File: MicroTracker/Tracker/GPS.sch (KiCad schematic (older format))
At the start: 27 parts, among them Q1 BC237, U2 GP.1575.15.4.B.02, U3 TPS22943, U8 BGA725L6, U9 TESEO-LIV3F

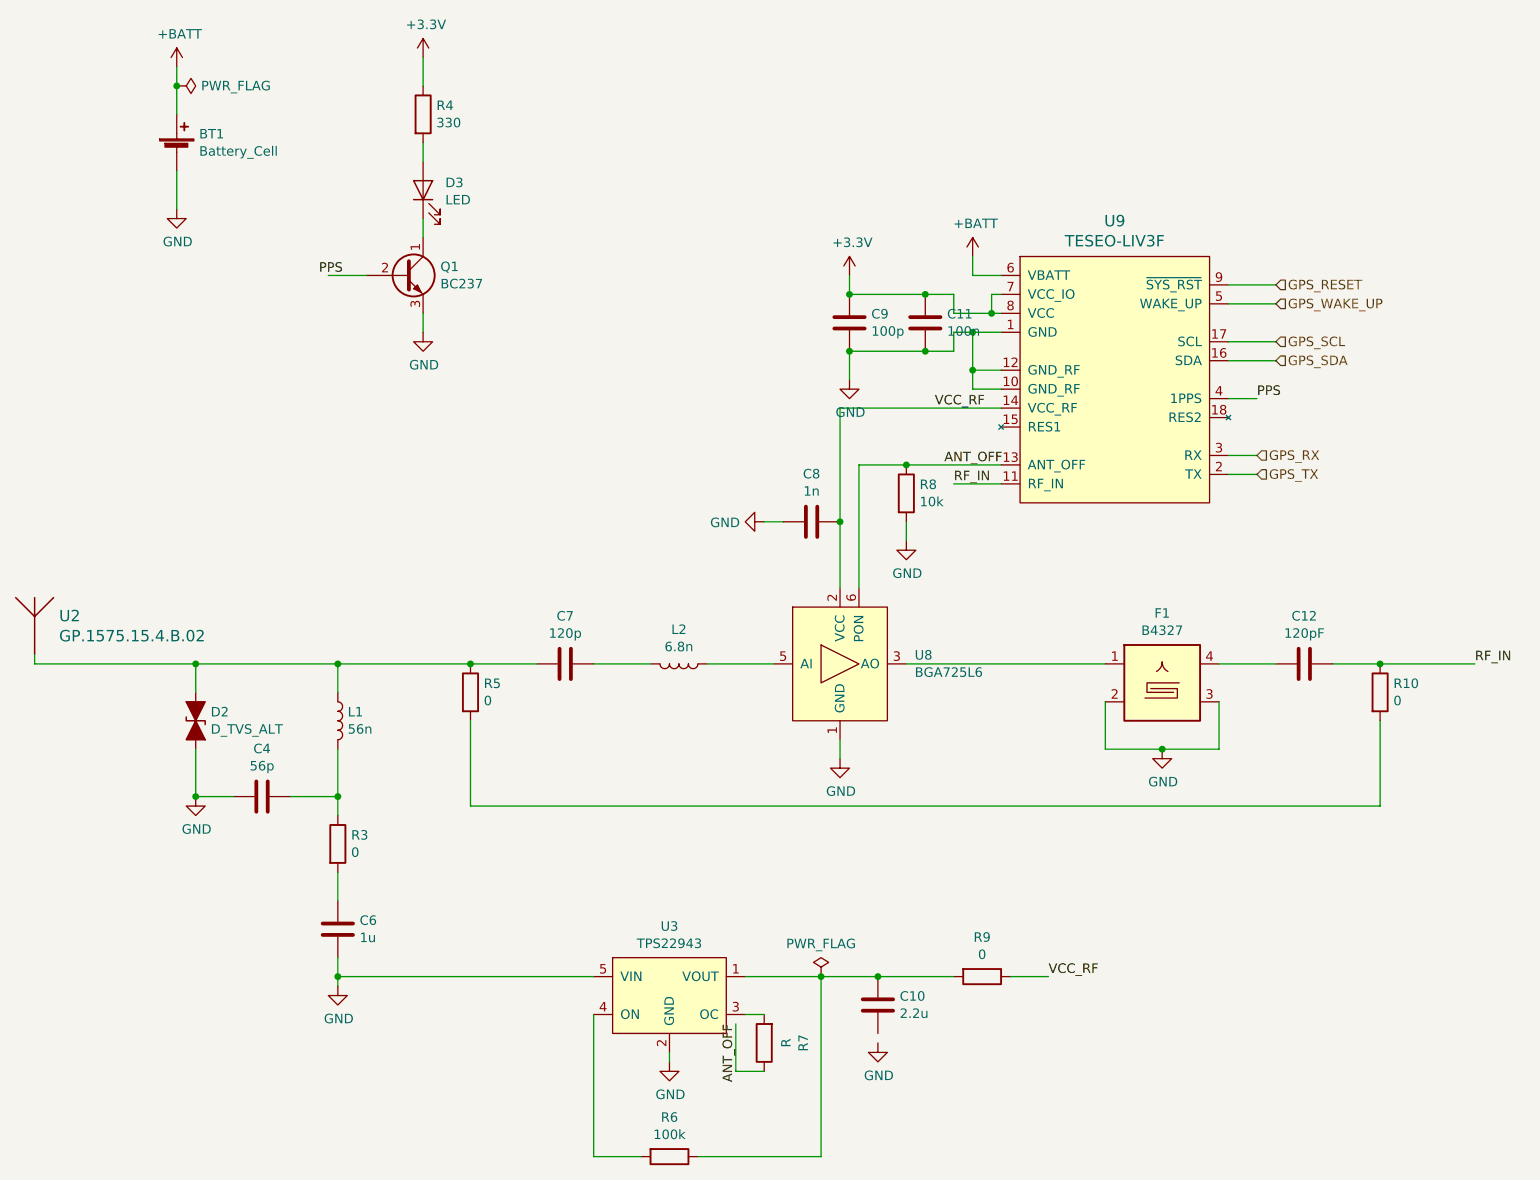
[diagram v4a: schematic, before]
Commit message: added more parts and lib
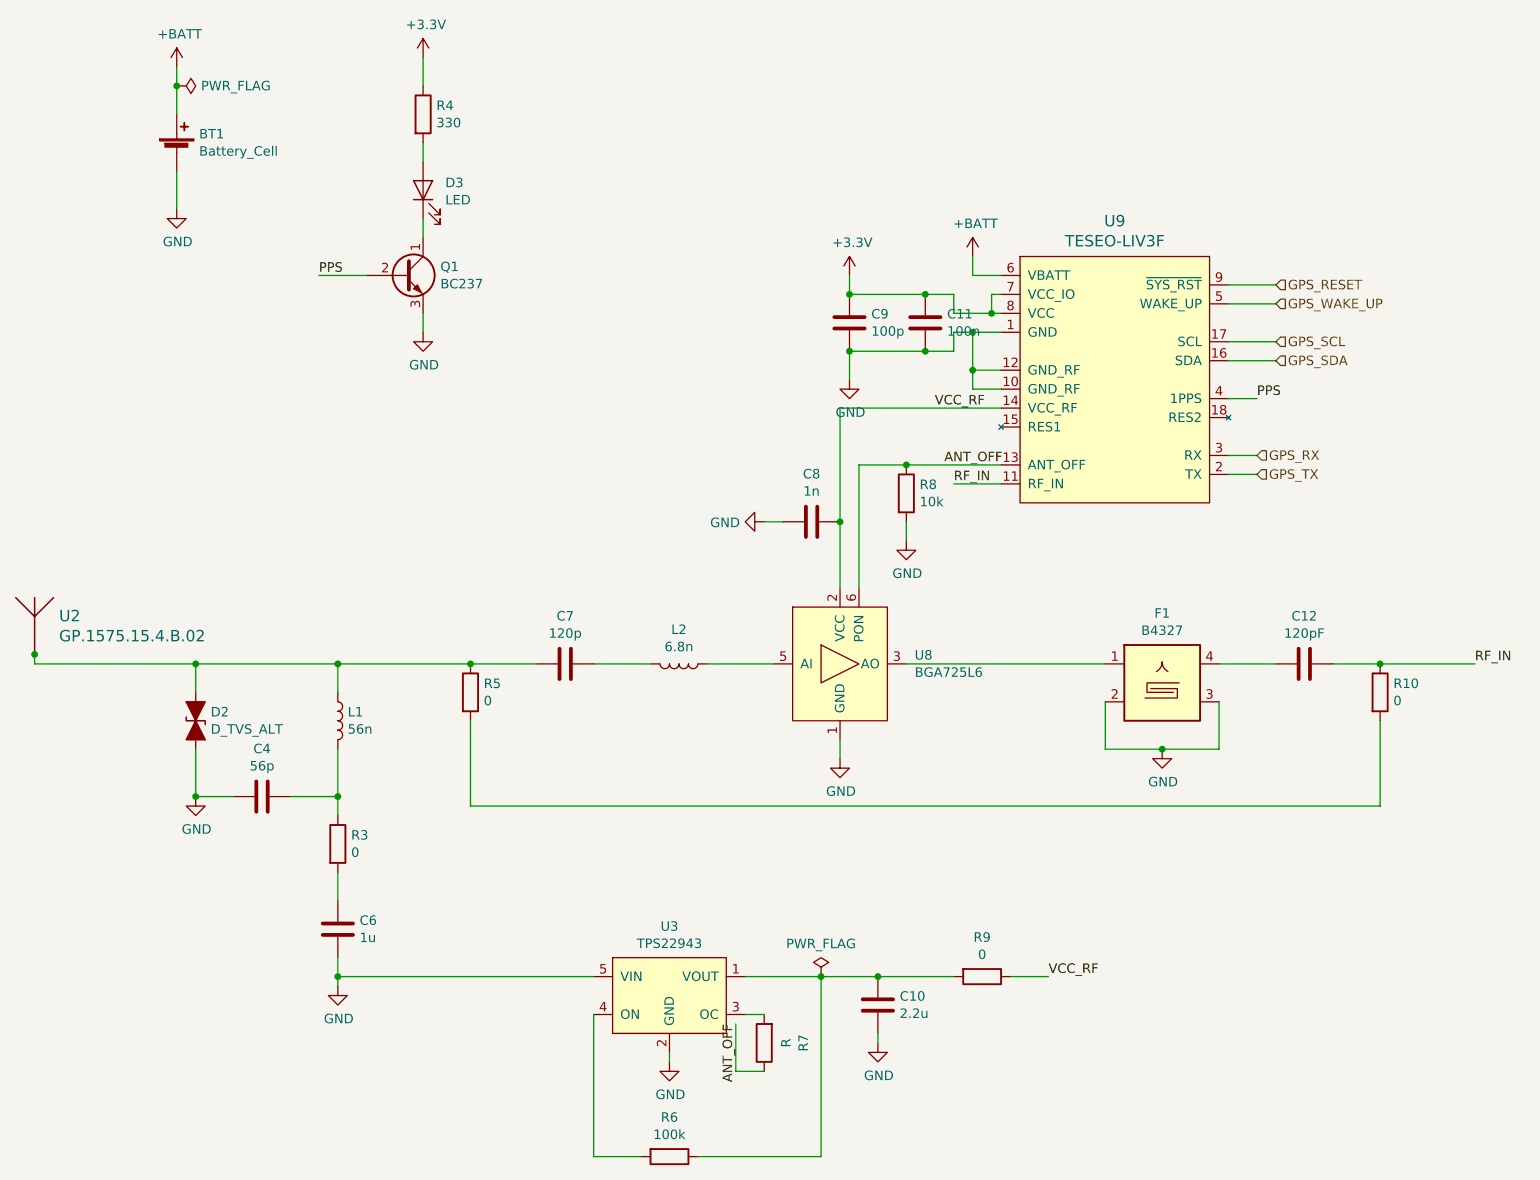
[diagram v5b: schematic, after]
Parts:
- U2: footprint GP.1575.15.4.B.02_TAL -> MicroTrackerPCBLib:GP.1575.15.4.B.02
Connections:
- net GND: now also C10.2
- net PPS: now also Q1.2 (B)
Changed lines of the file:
@@
 F 0 "U2" H 1079 4403 60  0000 L CNN
 F 1 "GP.1575.15.4.B.02" H 1079 4297 60  0000 L CNN
-F 2 "GP.1575.15.4.B.02_TAL" H 1725 2990 60  0001 C CNN
+F 2 "MicroTrackerPCBLib:GP.1575.15.4.B.02" H 1725 2990 60  0001 C CNN
 F 3 "" H 1050 4200 60  0000 C CNN
 	1    1050 4200
@@
 	3000 1900 3000 2000
 Wire Wire Line
-	2500 2200 2700 2200
-Wire Wire Line
 	3000 2400 3000 2500
 Text HLabel 7500 2250 2    50   Input ~ 0
@@
 Wire Wire Line
 	950  4200 950  4250
+Wire Wire Line
+	5400 6200 5400 6250
+Wire Wire Line
+	2450 2200 2700 2200
+Connection ~ 950  4200
 $EndSCHEMATC

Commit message: fixed errors
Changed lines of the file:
@@
 	5100 5900 5400 5900
-Wire Wire Line
-	4700 5900 5100 5900
 Wire Wire Line
 	4450 6850 5100 6850
@@
 Wire Wire Line
 	2450 2200 2700 2200
-Connection ~ 950  4200
+Wire Wire Line
+	4700 5900 5100 5900
 $EndSCHEMATC
